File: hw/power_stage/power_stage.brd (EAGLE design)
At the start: 117 x 100 mm, 47 parts, among them IC1H MIC4420M, IC1L MIC4429M, IC2H MIC4420M, IC2L MIC4429M, J1 AC1, J2 AC2, J3 OUT1, J4 OUT2

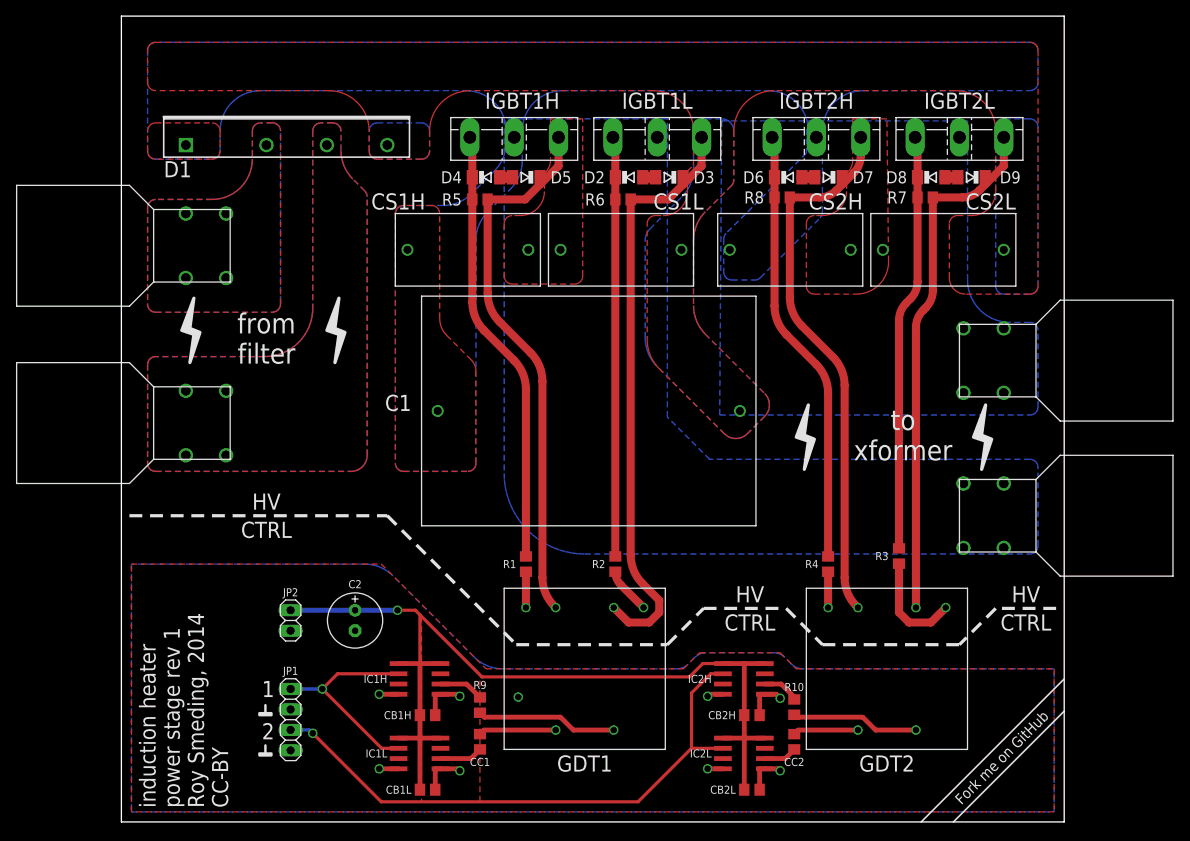
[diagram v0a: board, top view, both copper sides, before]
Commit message: Adapted power_stage.brd to be 100x100mm
This enables us to use cheap PCB fab services.
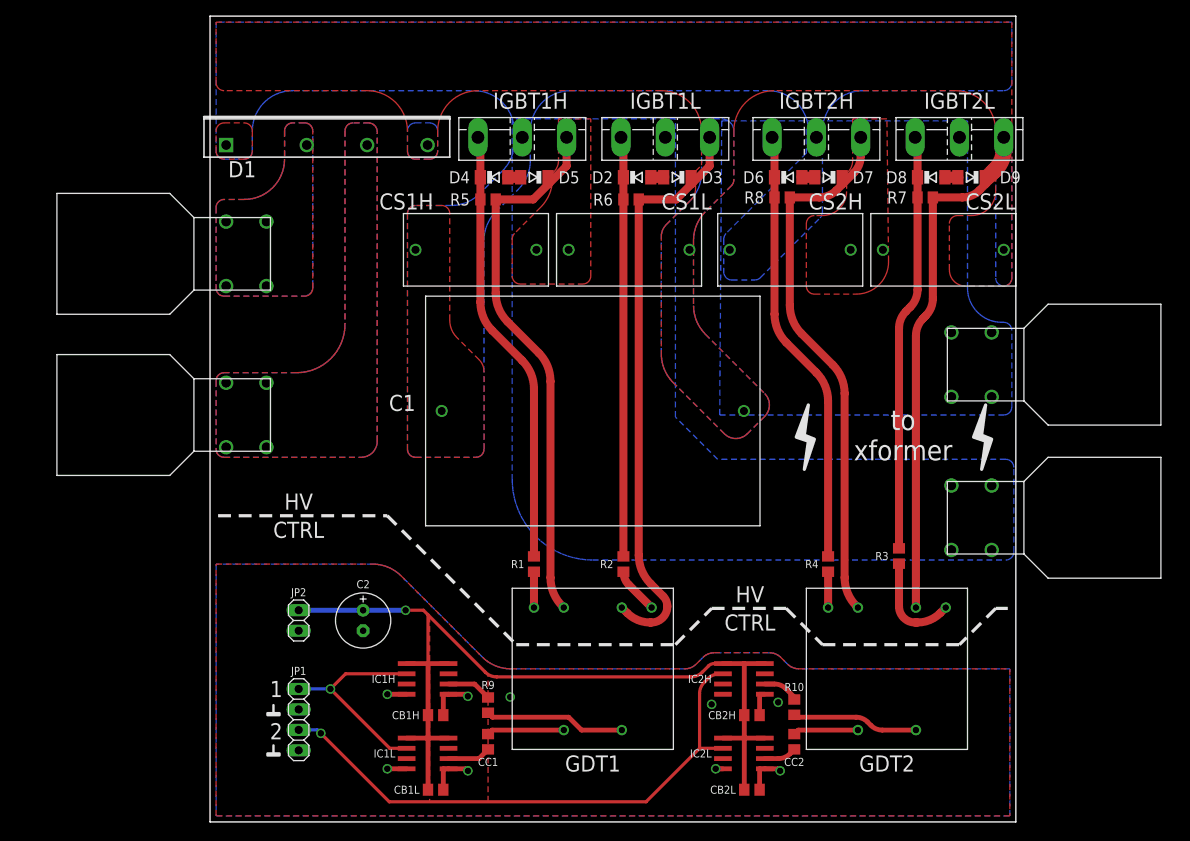
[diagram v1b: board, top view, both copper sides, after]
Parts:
- moved J1 5.10 mm to (7.50, 66.5)
- moved J2 5.10 mm to (7.50, 46.5)
- moved D1 5.00 mm to (18.8, 80.0)
- moved J4 1.58 mm to (97.5, 52.8)
- moved J3 1.52 mm to (97.5, 33.8)
- moved C2 1.00 mm to (22.0, 21.0)
- moved CB1H 1.00 mm to (31.0, 9.25)
- moved CB1L 1.00 mm to (31.0, 0.00)
- moved CC1 1.00 mm to (37.5, 5.95)
- moved CS1H 1.00 mm to (36.0, 67.0)
- moved CS1L 1.00 mm to (55.0, 67.0)
- moved D2 1.00 mm to (56.0, 76.0)
- moved D3 1.00 mm to (61.0, 76.0)
- moved D4 1.00 mm to (38.2, 76.0)
- moved D5 1.00 mm to (43.2, 76.0)
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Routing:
- net GND: track 30.8 -> 25.7 mm
- net N$20: track 71.8 -> 70.0 mm
- net VCC: track 115.9 -> 114.6 mm
- net V-: track 140.2 -> 139.2 mm
- net N$12: track 13.1 -> 12.4 mm
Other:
- board size 117 x 100 mm -> 100 x 100 mm
- board text removed: "Fork me on GitHub"
- board text removed: "from filter"
- board text removed: "induction heater power stage rev 1 Roy Smeding, 2014 CC-BY"

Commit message: Remove solder mask from high current tracks so we can cheaply increase their current capacity
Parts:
- removed J1: AC1, induction-heater:SCREW
- removed J2: AC2, induction-heater:SCREW
- removed R1, R2, R3, R4: (no value), rcl:R0805
- added AC1: AC1, induction-heater:SCREW
- added AC2: AC2, induction-heater:SCREW
- added RG1H, RG1L, RG2H, RG2L: (no value), rcl:R0805
- added TP_GDI1A, TP_GDI2B: A, testpad:TP10SQ
- added TP_GDI1B, TP_GDI2A: B, testpad:TP10SQ
- added TP_GNDA, TP_GNDB, TP_GNDC: GND, testpad:P1-13
- moved CB1L 0.25 mm to (31.0, 0.25)
- moved CS2H 0.25 mm to (74.8, 67.0)
- moved CS2L 0.25 mm to (93.8, 67.0)
- renumbered C1 to CF, C2 to CB, CC1 to CG1I, CC2 to CG2I, D1 to BR, D2 to DP1LA, D3 to DP1LB, D4 to DP1HA, D5 to DP1HB, D6 to DP2HA, D7 to DP2HB, D8 to DP2LA, D9 to DP2LB, J3 to OUT1, J4 to OUT2, R10 to RG2I, R5 to RP1H, R6 to RP1L, R7 to RP2L, R8 to RP2H, R9 to RG1I
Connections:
- net AC1: now also AC1.P$1, AC1.P$2, AC1.P$3, AC1.P$4; no longer J1.P$1, J1.P$2, J1.P$3, J1.P$4
- net AC2: now also AC2.P$1, AC2.P$2, AC2.P$3, AC2.P$4; no longer J2.P$1, J2.P$2, J2.P$3, J2.P$4
- net GND: now also TP_GNDA.TP, TP_GNDB.TP, TP_GNDC.TP
- net N$1: now also TP_GDI1B.TP
- net N$10: now also RG2L.2; no longer R3.2
- net N$11: now also RG1H.2; no longer R1.2
- net N$12: now also RG2L.1; no longer R3.1
- net N$13: now also RG2H.1; no longer R4.1
- net N$14: now also RG2H.2; no longer R4.2
- net N$26: now also TP_GDI1A.TP
- net N$27: now also TP_GDI2B.TP
- net N$3: now also RG1H.1; no longer R1.1
- net N$5: now also TP_GDI2A.TP
- net N$6: now also RG1L.2; no longer R2.2
- net N$7: now also RG1L.1; no longer R2.1
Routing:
- net N$27: track 8.11 -> 11.9 mm
- net N$5: track 15.8 -> 19.4 mm
- net N$26: track 9.61 -> 13.0 mm
- net N$1: track 17.5 -> 20.7 mm
- net N$14: track 54.3 -> 52.6 mm
- net N$11: track 54.3 -> 52.6 mm
- net GND: track 25.7 -> 26.9 mm, vias 9 -> 26
- net OUT1: track 68.1 -> 67.1 mm
- net N$3: track 4.45 -> 5.45 mm
- net N$13: track 4.45 -> 5.45 mm
- net N$6: track 52.1 -> 51.2 mm
- net N$7: track 5.76 -> 6.62 mm
- net OUT2: track 67.9 -> 67.0 mm
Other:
- board text added: "AC1"
- board text added: "AC2"
- board text added: "from mains"

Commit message: More fiddling
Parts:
- JP1: value input -> control
- moved RG2L 7.00 mm to (81.6, 29.0)
- moved CB 6.00 mm to (16.0, 21.0)
- moved OUT1 6.00 mm to (91.5, 33.8)
- moved OUT2 6.00 mm to (91.5, 52.8)
- moved CB1H 5.51 mm to (25.5, 9.50)
- moved CB2H 5.51 mm to (64.8, 9.50)
- moved CB2L 5.51 mm to (64.8, 0.25)
- moved CB1L 5.50 mm to (25.5, 0.25)
- moved AC1 5.00 mm to (4.50, 66.5)
- moved AC2 5.00 mm to (4.50, 46.5)
- moved BR 5.00 mm to (13.8, 80.0)
- moved CF 5.00 mm to (45.5, 47.0)
- moved CG1I 5.00 mm to (32.5, 5.95)
- moved CG2I 5.00 mm to (70.5, 5.95)
- moved CS1H 5.00 mm to (31.0, 67.0)
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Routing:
- net GND: track 26.9 -> 1.55 mm, vias 26 -> 47
- net V-: track 139.4 -> 140.7 mm
- net N$10: track 51.6 -> 52.5 mm
- net N$12: track 12.6 -> 13.4 mm
- net VCC: track 114.6 -> 115.3 mm
- removed copper zone on layer 1, net N$8
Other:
- board text added: "ac"
- board text added: "induction heater power stage revision 1 by Roy Smeding March 2015, CC-BY"
- board text added: "out"
